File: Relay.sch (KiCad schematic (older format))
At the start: 0 parts

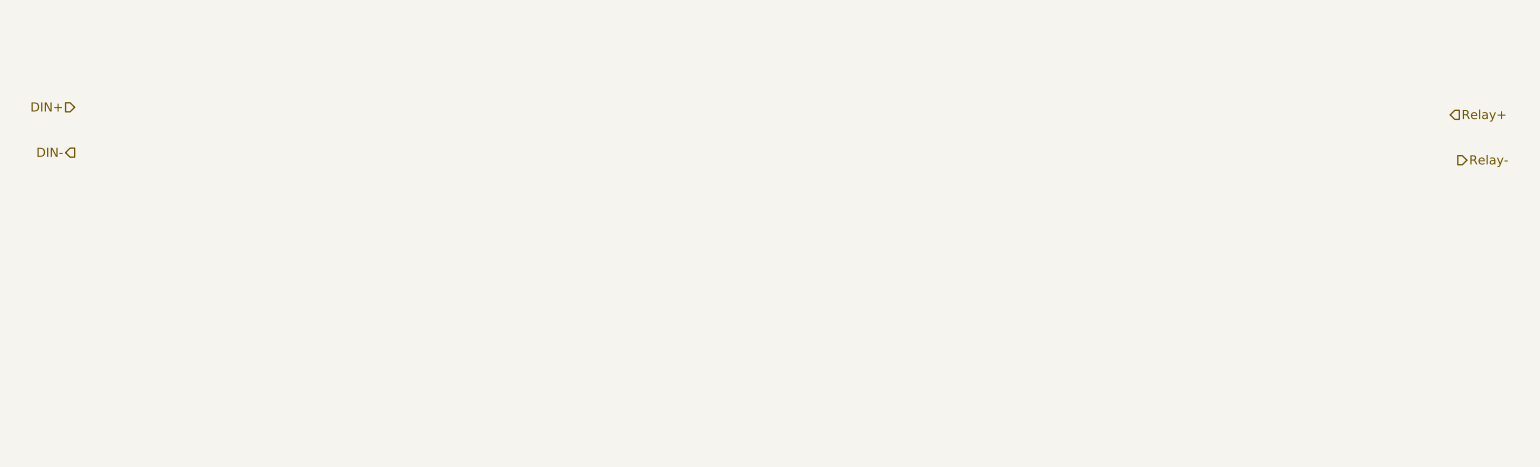
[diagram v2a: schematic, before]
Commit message: Completed Relay Module
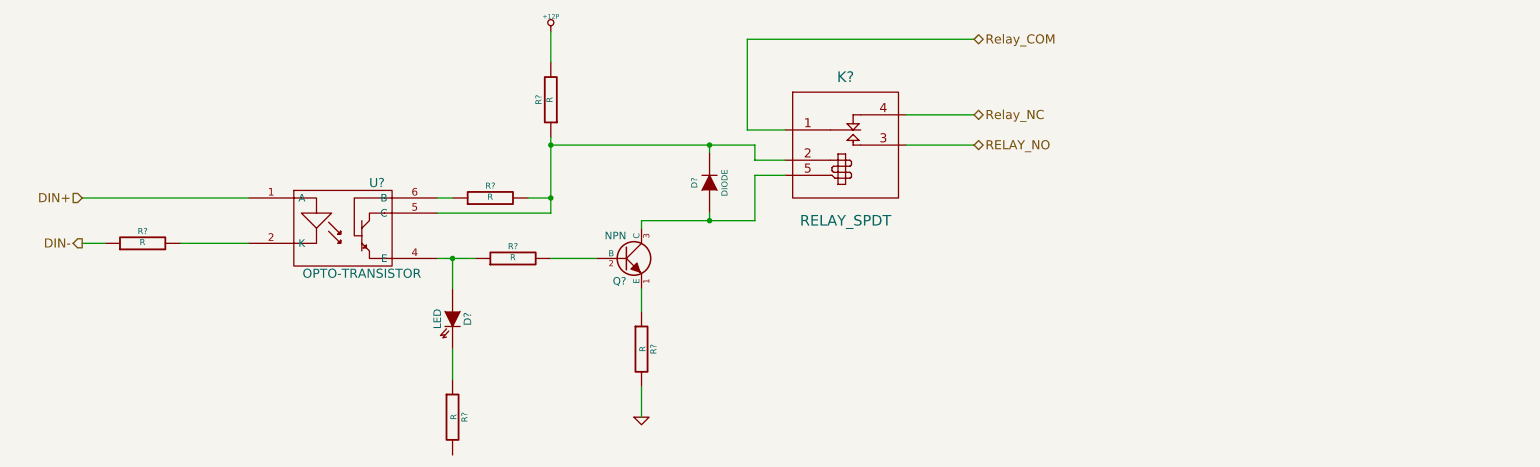
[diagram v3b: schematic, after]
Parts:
- added D?: LED, ~, symbol LED
- added D?: DIODE, ~, symbol DIODE
- added K?: RELAY_SPDT, ~, symbol RELAY_SPDT
- added Q?: NPN, ~, symbol NPN
- added R? (x6): R, ~, symbol R
- added U?: OPTO-TRANSISTOR, symbol OPTO-TRANSISTOR
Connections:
- net DIN+: now also U?.1 (A)
- net DIN-: now also R?.1
- new net: R?.2, U?.2 (K)
- new net: D?.1 (A), R?.1, U?.4 (E)
- new net: D?.2 (K), K?.2 (COIL+), R?.1, R?.2, U?.5 (C)
- new net: R?.1, U?.6 (B)
- new net: Q?.2 (B), R?.2
- new net: D?.2 (K), R?.1
- new net: Q?.1 (E), R?.1
- new net: D?.1 (A), K?.5 (COIL-), Q?.3 (C)
- new net +12P: R?.2
- new net GND: R?.2
- new net RELAY_NO: K?.3 (NO)
- new net Relay_COM: K?.1 (COM)
- new net Relay_NC: K?.4 (NC)
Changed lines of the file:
@@
 LIBS:contrib
 LIBS:valves
+LIBS:BenchBuddy
 LIBS:BenchBuddy-cache
 EELAYER 27 0
@@
 $Descr A4 11693 8268
 encoding utf-8
-Sheet 4 8
+Sheet 3 8
 Title ""
-Date "23 sep 2013"
+Date "4 oct 2013"
 Rev ""
 Comp ""
@@
 Comment4 ""
 $EndDescr
-Text HLabel 1350 2000 0    60   Input ~ 0
+Text HLabel 1400 2600 0    60   Input ~ 0
 DIN+
-Text HLabel 1350 2300 0    60   Output ~ 0
+Text HLabel 1400 2900 0    60   Output ~ 0
 DIN-
-Text HLabel 10450 2050 2    60   Input ~ 0
-Relay+
-Text HLabel 10500 2350 2    60   Output ~ 0
-Relay-
+Text HLabel 7300 2050 2    60   BiDi ~ 0
+Relay_NC
+Text HLabel 7300 2250 2    60   BiDi ~ 0
+RELAY_NO
+$Comp
+L OPTO-TRANSISTOR U?
+U 1 1 524E09FD
+P 3150 2800
+F 0 "U?" H 3350 3100 60  0000 C CNN
+F 1 "OPTO-TRANSISTOR" H 3250 2500 60  0000 C CNN
+F 2 "" H 3150 2800 60  0000 C CNN
+F 3 "" H 3150 2800 60  0000 C CNN
+	1    3150 2800
+	1    0    0    -1
+$EndComp
+$Comp
+L R R?
+U 1 1 524E0A0C
+P 4250 3000
+F 0 "R?" V 4330 3000 40  0000 C CNN
+F 1 "R" V 4257 3001 40  0000 C CNN
+F 2 "~" V 4180 3000 30  0000 C CNN
+F 3 "~" H 4250 3000 30  0000 C CNN
+	1    4250 3000
+	0    -1   -1   0
+$EndComp
+$Comp
+L LED D?
+U 1 1 524E0A1B
+P 3850 3400
+F 0 "D?" H 3850 3500 50  0000 C CNN
+F 1 "LED" H 3850 3300 50  0000 C CNN
+F 2 "~" H 3850 3400 60  0000 C CNN
+F 3 "~" H 3850 3400 60  0000 C CNN
+	1    3850 3400
+	0    1    1    0
+$EndComp
+$Comp
+L NPN Q?
+U 1 1 524E0A2A
+P 5000 3000
+F 0 "Q?" H 5000 2850 50  0000 R CNN
+F 1 "NPN" H 5000 3150 50  0000 R CNN
+F 2 "~" H 5000 3000 60  0000 C CNN
+F 3 "~" H 5000 3000 60  0000 C CNN
+	1    5000 3000
+	1    0    0    -1
+$EndComp
+$Comp
+L RELAY_SPDT K?
+U 1 1 524E1098
+P 6450 2250
+F 0 "K?" H 6450 2700 70  0000 C CNN
+F 1 "RELAY_SPDT" H 6450 1750 70  0000 C CNN
+F 2 "~" H 6450 2400 60  0000 C CNN
+F 3 "~" H 6450 2400 60  0000 C CNN
+	1    6450 2250
+	1    0    0    -1
+$EndComp
+Text HLabel 7300 1550 2    60   BiDi ~ 0
+Relay_COM
+$Comp
+L R R?
+U 1 1 524E1117
+P 5100 3600
+F 0 "R?" V 5180 3600 40  0000 C CNN
+F 1 "R" V 5107 3601 40  0000 C CNN
+F 2 "~" V 5030 3600 30  0000 C CNN
+F 3 "~" H 5100 3600 30  0000 C CNN
+	1    5100 3600
+	1    0    0    -1
+$EndComp
+$Comp
+L GND #PWR?
+U 1 1 524E112A
+P 5100 4050
+F 0 "#PWR?" H 5100 4050 30  0001 C CNN
+F 1 "GND" H 5100 3980 30  0001 C CNN
+F 2 "~" H 5100 4050 60  0000 C CNN
+F 3 "~" H 5100 4050 60  0000 C CNN
+	1    5100 4050
+	1    0    0    -1
+$EndComp
+$Comp
+L R R?
+U 1 1 524E1143
+P 3850 4050
+F 0 "R?" V 3930 4050 40  0000 C CNN
+F 1 "R" V 3857 4051 40  0000 C CNN
+F 2 "~" V 3780 4050 30  0000 C CNN
+F 3 "~" H 3850 4050 30  0000 C CNN
+	1    3850 4050
+	1    0    0    -1
+$EndComp
+$Comp
+L +12P #PWR?
+U 1 1 524E118A
+P 4500 1500
+F 0 "#PWR?" H 4500 1470 30  0001 C CNN
+F 1 "+12P" H 4500 1600 30  0000 C CNN
+F 2 "~" H 4500 1500 60  0000 C CNN
+F 3 "~" H 4500 1500 60  0000 C CNN
+	1    4500 1500
+	1    0    0    -1
+$EndComp
+Wire Wire Line
+	1400 2600 2500 2600
+Wire Wire Line
+	2050 2900 2500 2900
+Wire Wire Line
+	7300 2050 6850 2050
+Wire Wire Line
+	7300 2250 6850 2250
+Wire Wire Line
+	7300 1550 5800 1550
+Wire Wire Line
+	5800 1550 5800 2150
+Wire Wire Line
+	5800 2150 6050 2150
+Wire Wire Line
+	4500 3000 4800 3000
+Wire Wire Line
+	5100 3200 5100 3350
+Wire Wire Line
+	5100 3850 5100 4050
+Wire Wire Line
+	3750 3000 4000 3000
+Wire Wire Line
+	3850 3200 3850 3000
+Connection ~ 3850 3000
+Wire Wire Line
+	3850 3800 3850 3600
+$Comp
+L R R?
+U 1 1 524E11AA
+P 4500 1950
+F 0 "R?" V 4580 1950 40  0000 C CNN
+F 1 "R" V 4507 1951 40  0000 C CNN
+F 2 "~" V 4430 1950 30  0000 C CNN
+F 3 "~" H 4500 1950 30  0000 C CNN
+	1    4500 1950
+	-1   0    0    1
+$EndComp
+Wire Wire Line
+	5850 2350 6050 2350
+$Comp
+L R R?
+U 1 1 524E11D3
+P 4100 2600
+F 0 "R?" V 4180 2600 40  0000 C CNN
+F 1 "R" V 4107 2601 40  0000 C CNN
+F 2 "~" V 4030 2600 30  0000 C CNN
+F 3 "~" H 4100 2600 30  0000 C CNN
+	1    4100 2600
+	0    -1   -1   0
+$EndComp
+Wire Wire Line
+	3750 2600 3850 2600
+Wire Wire Line
+	4500 2700 3750 2700
+Wire Wire Line
+	4500 2200 4500 2700
+Wire Wire Line
+	4350 2600 4500 2600
+Connection ~ 4500 2600
+Wire Wire Line
+	4500 1700 4500 1500
+$Comp
+L R R?
+U 1 1 524E1262
+P 1800 2900
+F 0 "R?" V 1880 2900 40  0000 C CNN
+F 1 "R" V 1807 2901 40  0000 C CNN
+F 2 "~" V 1730 2900 30  0000 C CNN
+F 3 "~" H 1800 2900 30  0000 C CNN
+	1    1800 2900
+	0    -1   -1   0
+$EndComp
+Wire Wire Line
+	1400 2900 1550 2900
+$Comp
+L DIODE D?
+U 1 1 524E12D3
+P 5550 2500
+F 0 "D?" H 5550 2600 40  0000 C CNN
+F 1 "DIODE" H 5550 2400 40  0000 C CNN
+F 2 "~" H 5550 2500 60  0000 C CNN
+F 3 "~" H 5550 2500 60  0000 C CNN
+	1    5550 2500
+	0    -1   -1   0
+$EndComp
+Wire Wire Line
+	6050 2450 5850 2450
+Wire Wire Line
+	5850 2450 5850 2750
+Wire Wire Line
+	5850 2250 5850 2350
+Wire Wire Line
+	4500 2250 5850 2250
+Connection ~ 4500 2250
+Wire Wire Line
+	5550 2300 5550 2250
+Connection ~ 5550 2250
+Wire Wire Line
+	5850 2750 5100 2750
+Wire Wire Line
+	5100 2750 5100 2800
+Wire Wire Line
+	5550 2700 5550 2750
+Connection ~ 5550 2750
 $EndSCHEMATC

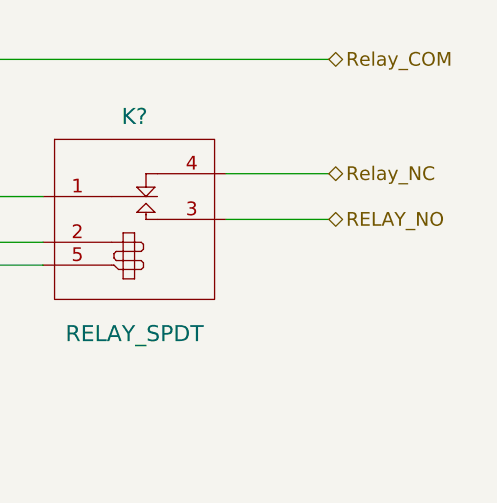
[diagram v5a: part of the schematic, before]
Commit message: Added connections to Terminal Block
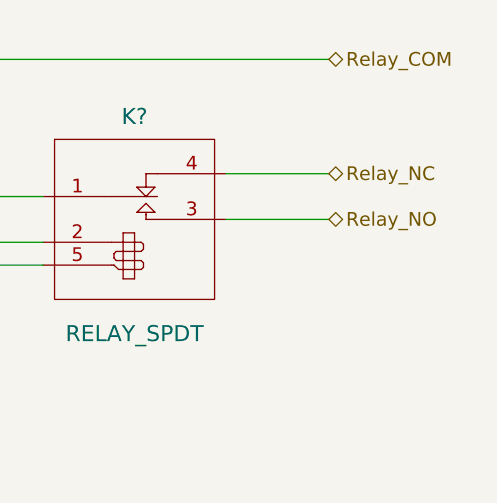
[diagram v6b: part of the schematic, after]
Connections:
- net RELAY_NO renamed Relay_NO
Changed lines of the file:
@@
 Relay_NC
 Text HLabel 7300 2250 2    60   BiDi ~ 0
-RELAY_NO
+Relay_NO
 $Comp
 L OPTO-TRANSISTOR U?

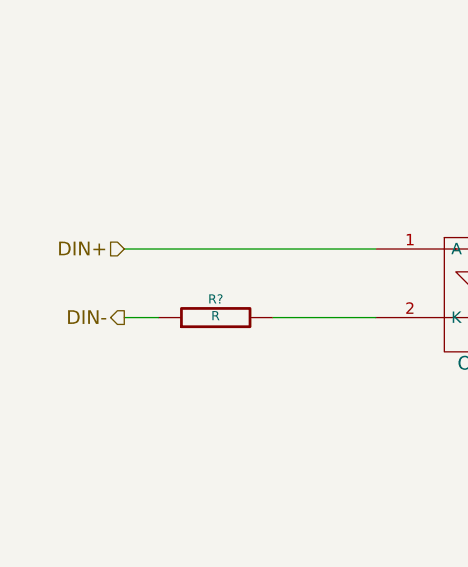
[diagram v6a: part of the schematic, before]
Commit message: Arduino Module Connection
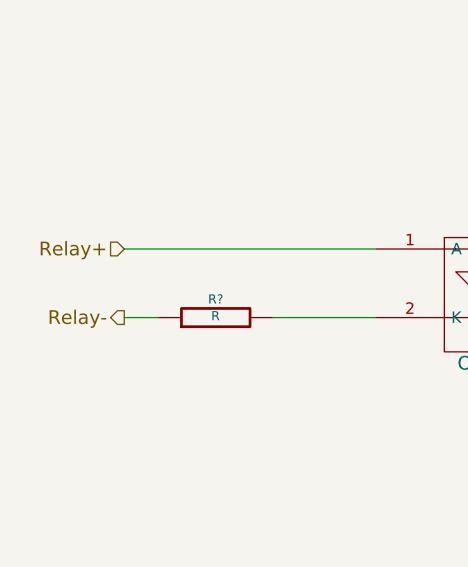
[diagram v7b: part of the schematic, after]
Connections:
- net DIN+ renamed Relay+
- net DIN- renamed Relay-
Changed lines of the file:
@@
 Sheet 3 9
 Title ""
-Date "11 oct 2013"
+Date "22 oct 2013"
 Rev ""
 Comp ""
@@
 $EndDescr
 Text HLabel 1400 2600 0    60   Input ~ 0
-DIN+
+Relay+
 Text HLabel 1400 2900 0    60   Output ~ 0
-DIN-
+Relay-
 Text HLabel 7300 2050 2    60   BiDi ~ 0
 Relay_NC
